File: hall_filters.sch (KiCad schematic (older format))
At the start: 11 parts

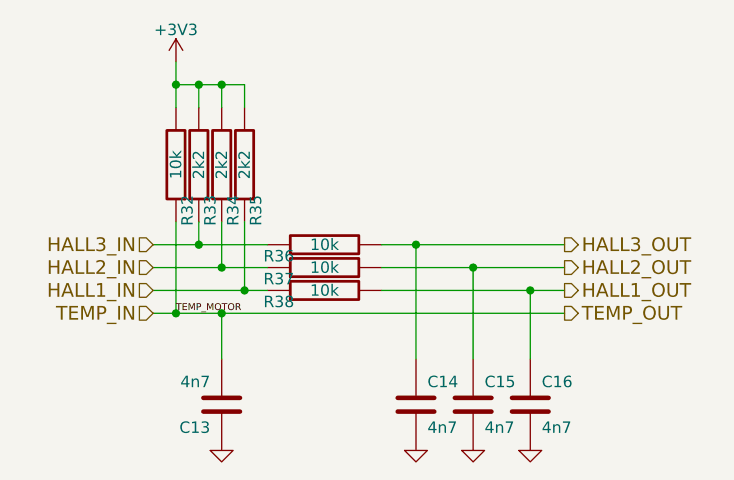
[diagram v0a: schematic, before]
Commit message: - removed lots of unused circuitry - implemented new DMOS power stage - power supplies still missing - removed rescue lib and fixed referenced
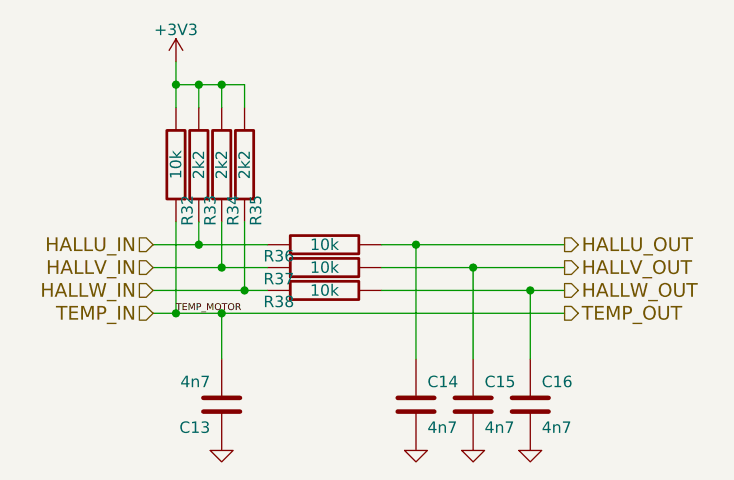
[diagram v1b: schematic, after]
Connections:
- net HALL1_IN renamed HALLW_IN
- net HALL1_OUT renamed HALLW_OUT
- net HALL2_IN renamed HALLV_IN
- net HALL2_OUT renamed HALLV_OUT
- net HALL3_IN renamed HALLU_IN
- net HALL3_OUT renamed HALLU_OUT
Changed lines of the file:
@@
 $Descr A4 11693 8268
 encoding utf-8
-Sheet 3 7
+Sheet 3 6
 Title "HSWR HAL Filters"
 Date "2017-02-05"
@@
 Connection ~ 5100 3850
 Text HLabel 4800 3550 0    60   Input ~ 0
-HALL3_IN
+HALLU_IN
 Text HLabel 4800 3650 0    60   Input ~ 0
-HALL2_IN
+HALLV_IN
 Text HLabel 4800 3750 0    60   Input ~ 0
-HALL1_IN
+HALLW_IN
 Text HLabel 4800 3850 0    60   Input ~ 0
 TEMP_IN
 Text HLabel 6600 3550 2    60   Output ~ 0
-HALL3_OUT
+HALLU_OUT
 Text HLabel 6600 3650 2    60   Output ~ 0
-HALL2_OUT
+HALLV_OUT
 Text HLabel 6600 3750 2    60   Output ~ 0
-HALL1_OUT
+HALLW_OUT
 Text HLabel 6600 3850 2    60   Output ~ 0
 TEMP_OUT
